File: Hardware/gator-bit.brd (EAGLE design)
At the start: 114.4 x 70.4 mm, 92 parts, among them J1 GATOR, J10 GATOR, J11 GATOR, J12 GATOR, J13 GATOR, J14 GATOR, J15 GATOR, J16 GATOR, J17 GATOR, J18 GATOR, J2 GATOR, J3 GATOR, J4 GATOR, J6 GATOR, J7 GATOR, J8 GATOR, J9 GATOR, U1 TPS63070, U2 micro:bit, U3 TXB0104, U4 ADJ REG 1.5A

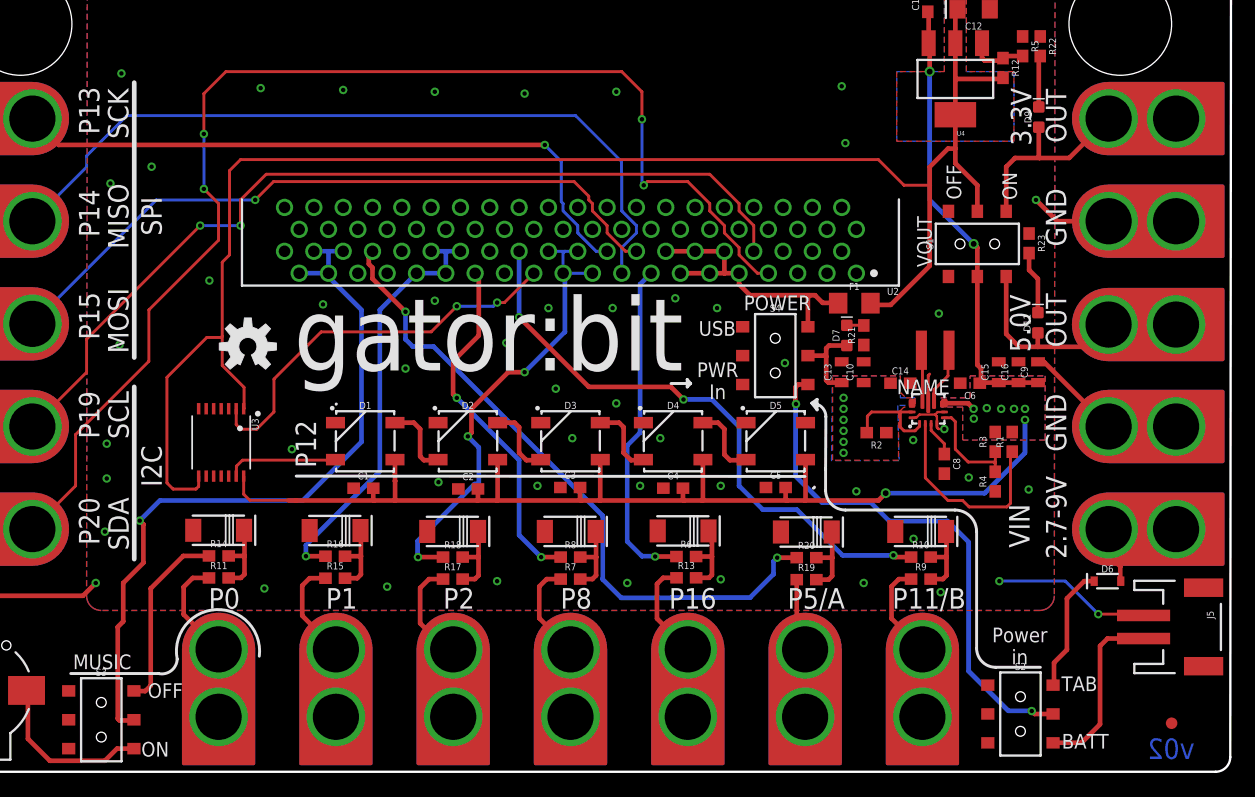
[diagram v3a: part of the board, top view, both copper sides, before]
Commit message: prop to vect text
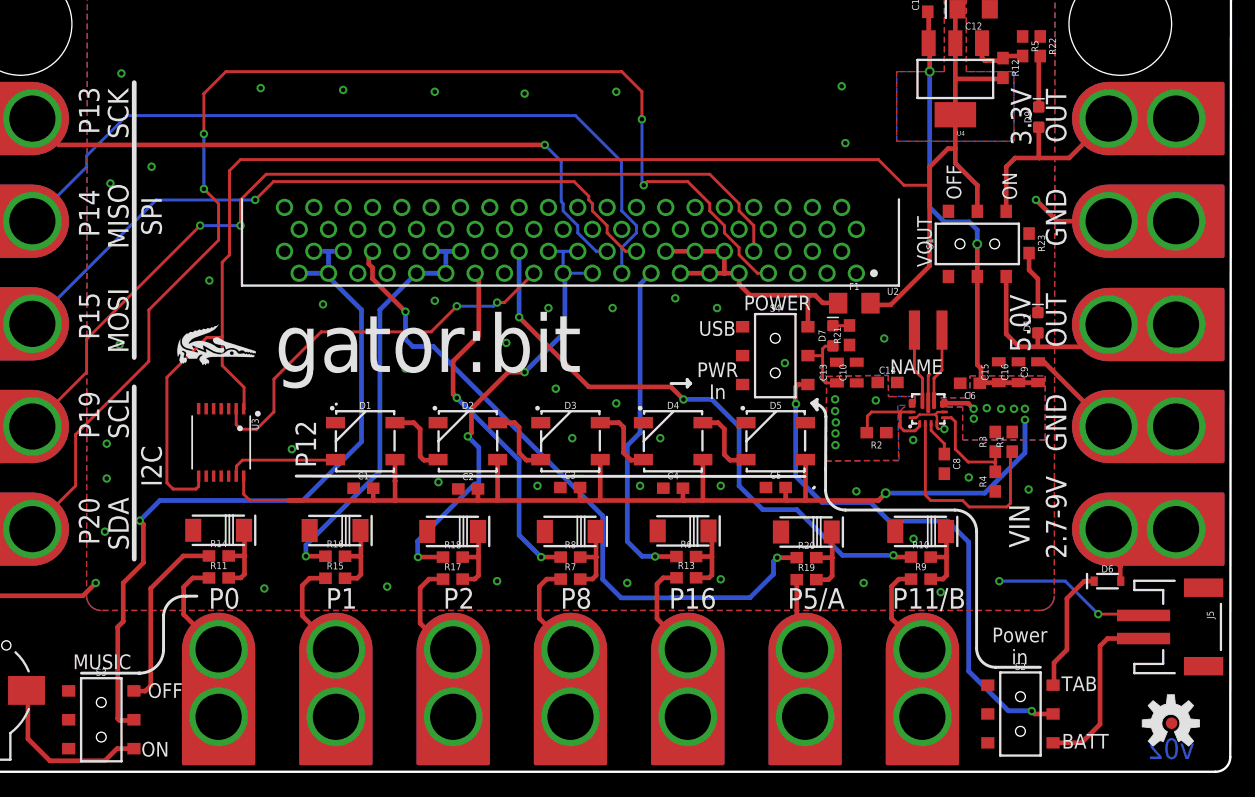
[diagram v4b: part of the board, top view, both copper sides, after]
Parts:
- moved LOGO2 86.4 mm to (109.2, 4.19)
- moved L1 1.85 mm to (88.1, 38.3)
- moved LOGO1 1.42 mm to (74.3, 16.5)
- moved R21 1.24 mm to (81.3, 37.8)
- moved D7 1.21 mm to (79.9, 37.8)
- moved C14 1.11 mm to (84.6, 33.7)
- moved C10 0.60 mm to (81.9, 34.6)
- moved C13 0.41 mm to (80.2, 34.6)
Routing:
- net N$2: track 4.40 -> 6.41 mm
- net N$8: track 4.90 -> 6.40 mm
- net 5V: track 140.0 -> 141.3 mm
- net VIN: track 8.27 -> 7.01 mm
- net N$14: track 17.8 -> 18.7 mm
